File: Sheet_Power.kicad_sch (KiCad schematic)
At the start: 31 parts, among them J2 USB_C_Receptacle_PowerOnly_6P, Q2 DMG2301L, SW1 SW_SPDT, U13 SC189LSKTRT, U14 TLV73312PDBV, U15 LD39200PUR, U16 TPS6208x, U21 TPD1E05U06DYA, U22 TLV73325PDBV

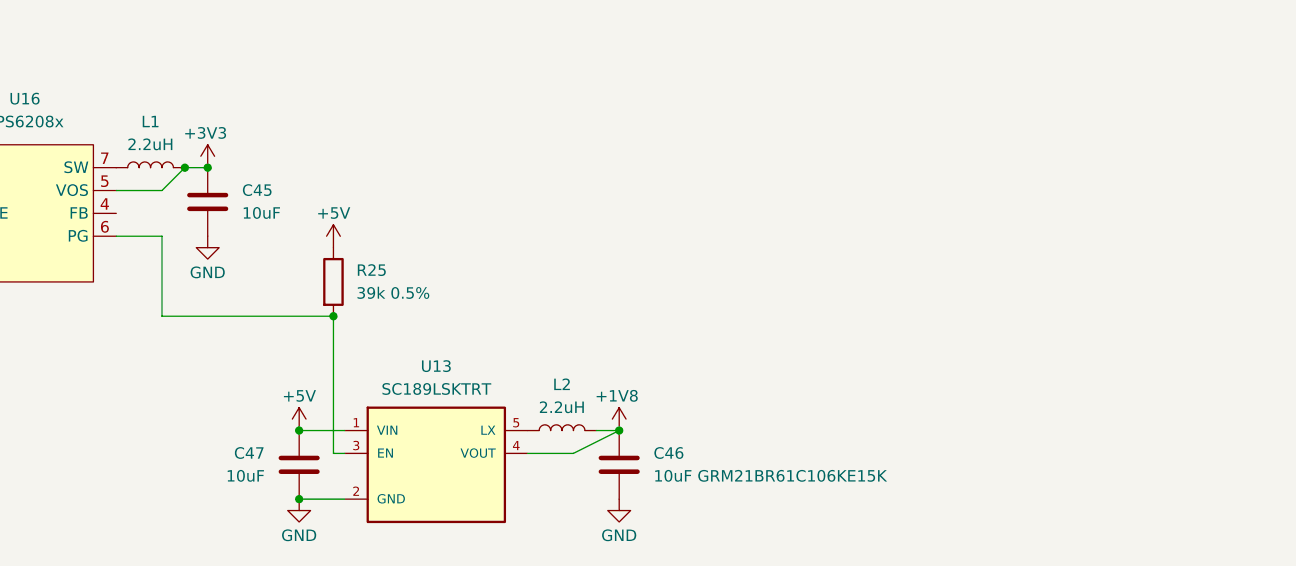
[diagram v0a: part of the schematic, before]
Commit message: added some capacitors to various components that weren't capacitored enough
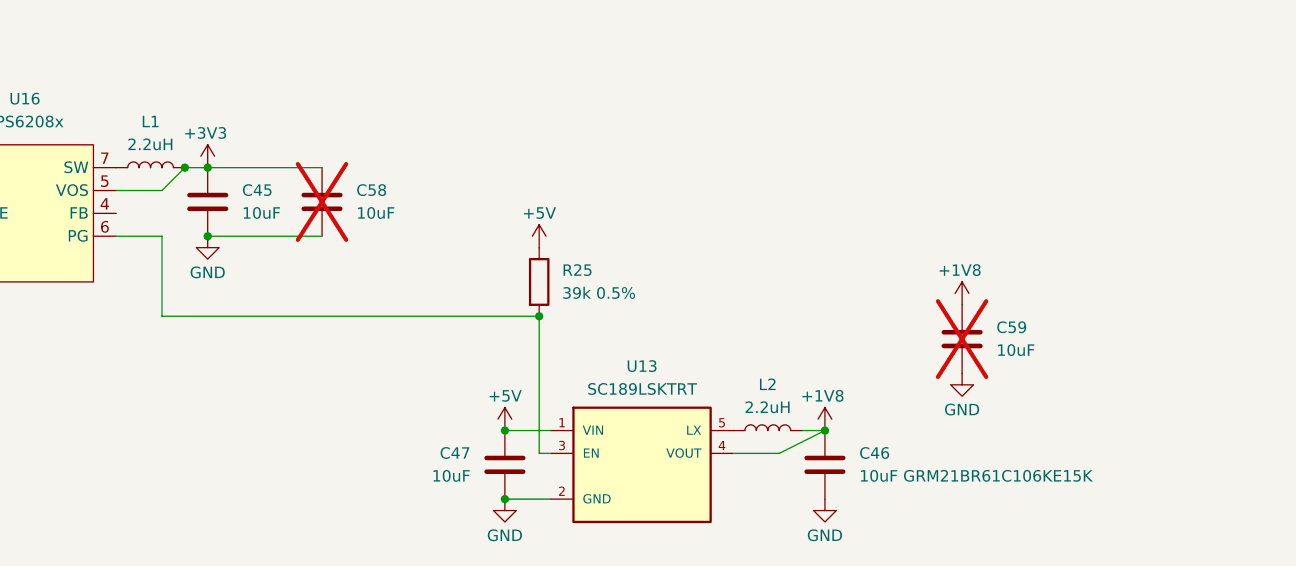
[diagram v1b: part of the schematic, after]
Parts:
- added C58, C59: 10uF, Capacitor_SMD:C_0603_1608Metric_Pad1.08x0.95mm_HandSolder, symbol Device:C
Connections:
- net +1V8: now also C59.1
- net +3V3: now also C58.1
- net GND: now also C58.2, C59.2
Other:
- moved on the sheet: C46, C47, L2, R25, U13
